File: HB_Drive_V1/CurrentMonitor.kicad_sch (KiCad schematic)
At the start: 0 parts

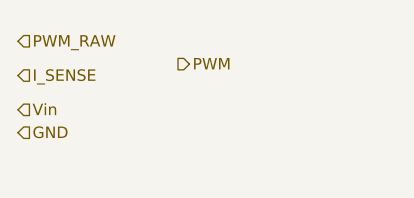
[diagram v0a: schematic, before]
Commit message: fixes git and adds a first revision of the Inner Current Regulator (NOT COMPLETE)
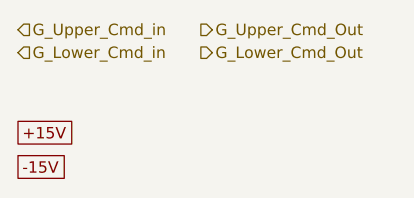
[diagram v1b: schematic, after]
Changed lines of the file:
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@@
 	(generator_version "10.0")
 	(paper "A4")
-	(hierarchical_label "GND"
+	(global_label "-15V"
+		(shape passive)
+		(at 88.9 87.63 0)
+		(fields_autoplaced yes)
+		(effects
+			(font
+				(size 1.27 1.27)
+			)
+			(justify left)
+		)
+		(property "Intersheetrefs" "${INTERSHEET_REFS}"
+			(at 95.8539 87.63 0)
+			(hide yes)
+			(show_name no)
+			(do_not_autoplace no)
+			(effects
+				(font
+					(size 1.27 1.27)
+				)
+				(justify left)
+			)
+		)
+	)
+	(global_label "+15V"
+		(shape passive)
+		(at 88.9 83.82 0)
+		(fields_autoplaced yes)
+		(effects
+			(font
+				(size 1.27 1.27)
+			)
+			(justify left)
+		)
+		(property "Intersheetrefs" "${INTERSHEET_REFS}"
+			(at 95.8539 83.82 0)
+			(hide yes)
+			(show_name no)
+			(do_not_autoplace no)
+			(effects
+				(font
+					(size 1.27 1.27)
+				)
+				(justify left)
+			)
+		)
+	)
+	(hierarchical_label "G_Lower_Cmd_in"
 		(shape input)
-		(at 88.9 83.82 0)
+		(at 88.9 74.93 0)
 		(effects
 			(font
@@
 		)
 	)
-	(hierarchical_label "I_SENSE"
-		(shape input)
-		(at 88.9 77.47 0)
+	(hierarchical_label "G_Lower_Cmd_Out"
+		(shape output)
+		(at 109.22 74.93 0)
 		(effects
 			(font
@@
 		)
 	)
-	(hierarchical_label "PWM_RAW"
+	(hierarchical_label "G_Upper_Cmd_in"
 		(shape input)
-		(at 88.9 73.66 0)
+		(at 88.9 72.39 0)
 		(effects
 			(font
@@
 		)
 	)
-	(hierarchical_label "Vin"
-		(shape input)
-		(at 88.9 81.28 0)
+	(hierarchical_label "G_Upper_Cmd_Out"
+		(shape output)
+		(at 109.22 72.39 0)
 		(effects
 			(font
-				(size 1.27 1.27)
-			)
-			(justify left)
-		)
-	)
-	(hierarchical_label "PWM"
-		(shape output)
-		(at 106.68 76.2 0)
-		(effects
-			(font

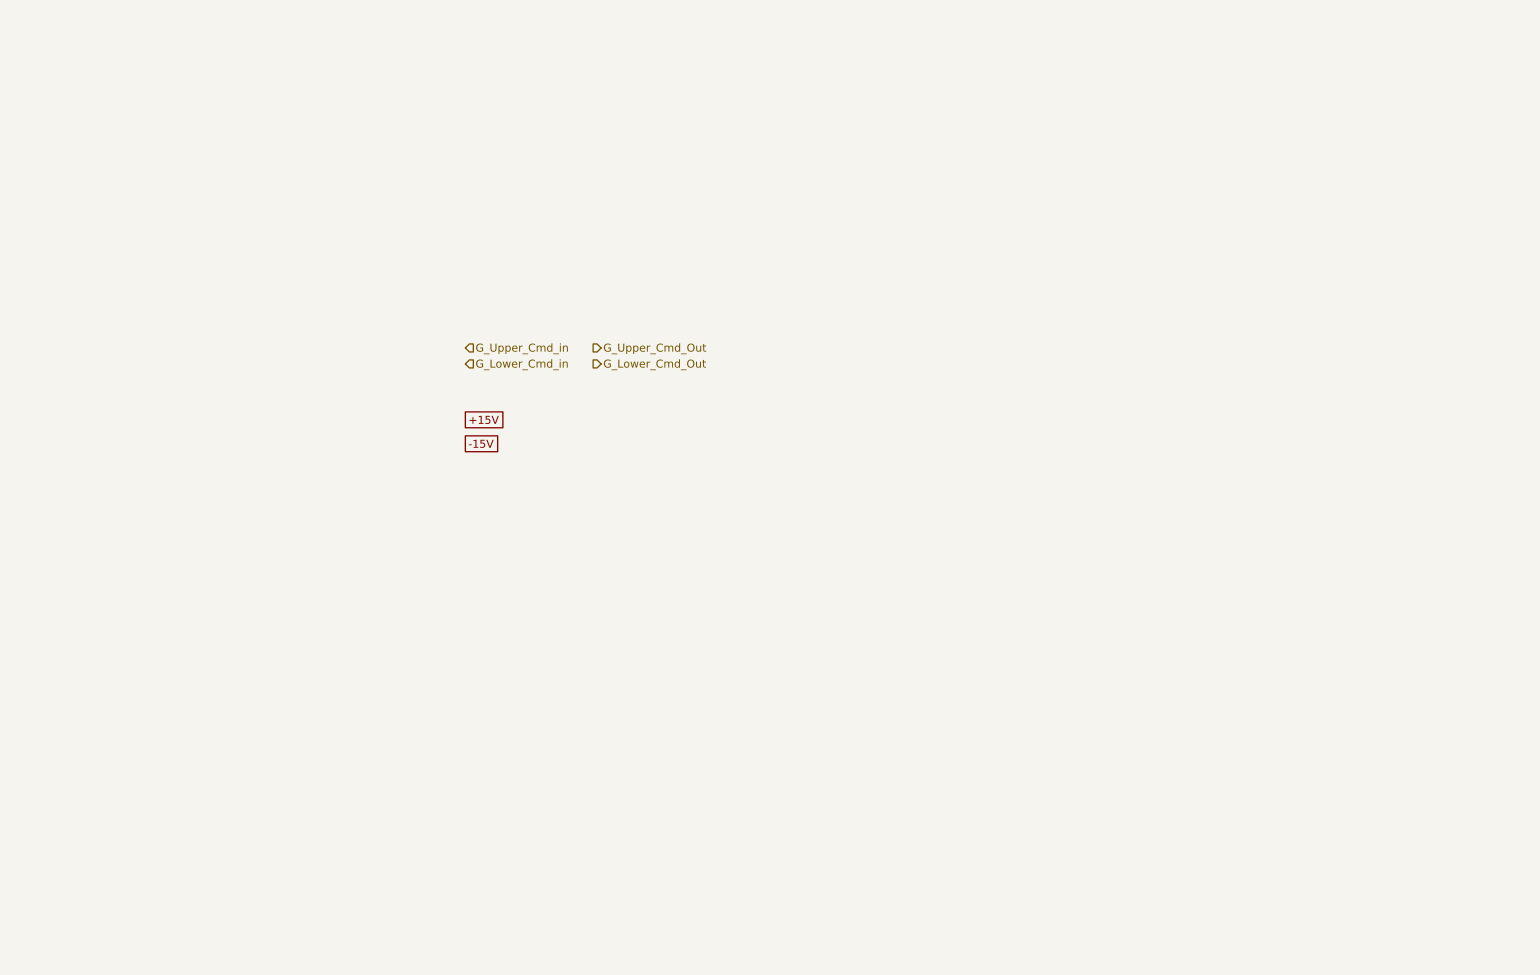
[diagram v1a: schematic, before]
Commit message: adds 10v reference and DC offsets / gain control to I_fdbk and V_fdbk
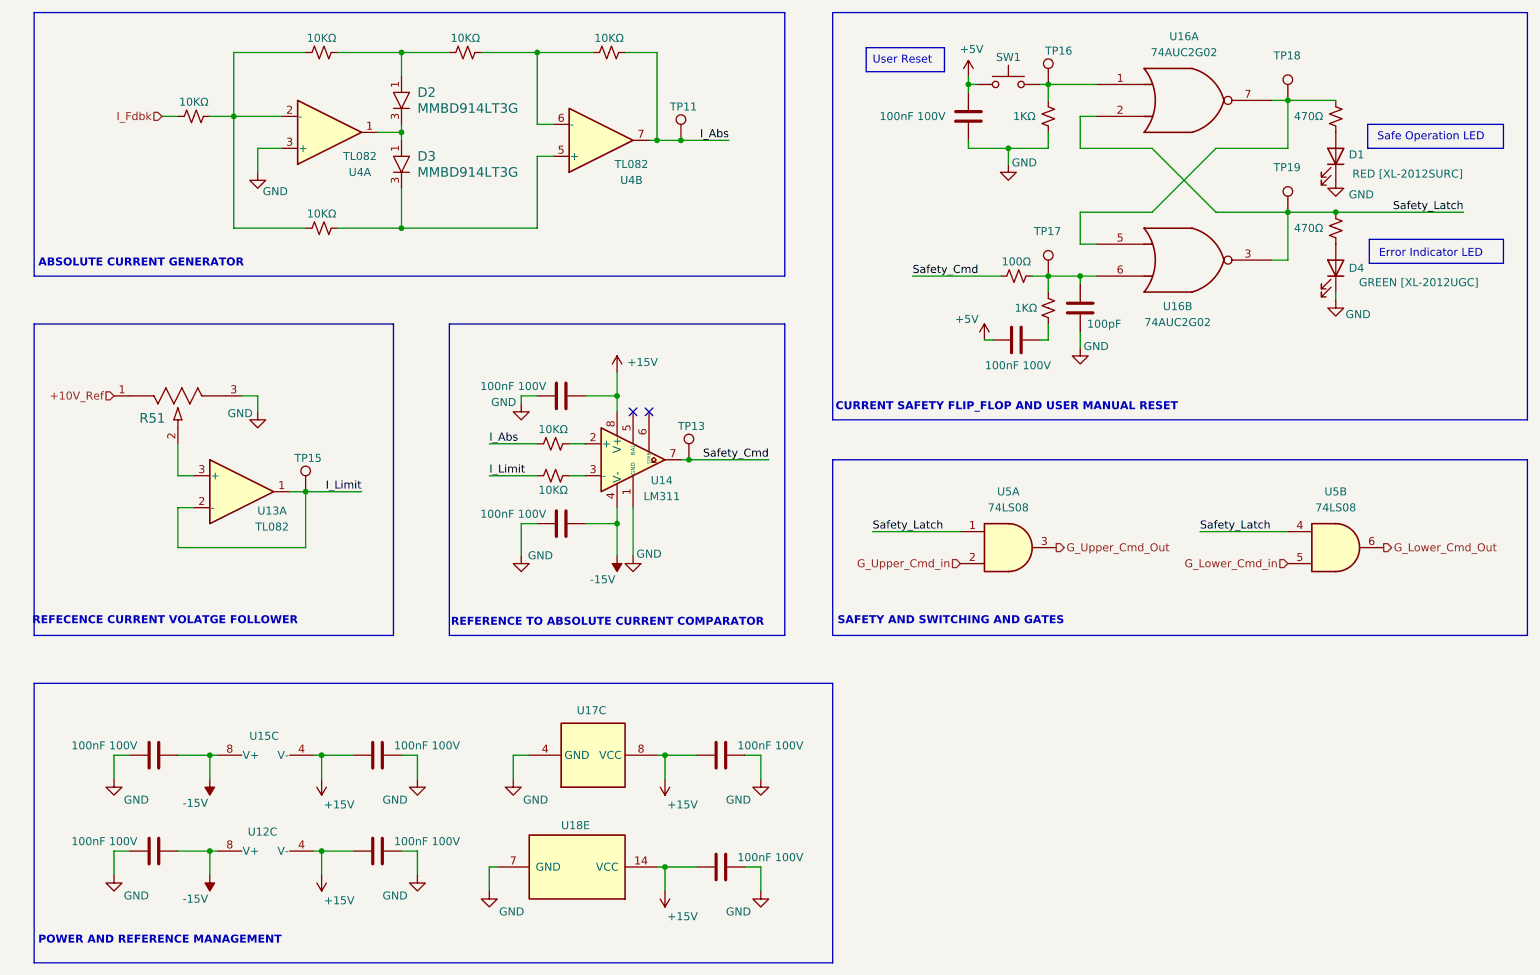
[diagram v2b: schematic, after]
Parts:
- added C25, C26, C28, C29, C30, C31, C34, C35, C36, C37: 100nF 100V, Capacitor_SMD:C_0603_1608Metric, symbol Device:C
- added C32: 100pF, Capacitor_SMD:C_0603_1608Metric, symbol Device:C
- added D1: RED [XL-2012SURC], LED_SMD:LED_0805_2012Metric_Pad1.15x1.40mm_HandSolder, symbol Device:LED
- added D2, D3: MMBD914LT3G, Package_TO_SOT_SMD:SOT-23-3, symbol MMBD914LT3G:MMBD914LT3G
- added D4: GREEN [XL-2012UGC], LED_SMD:LED_0805_2012Metric_Pad1.15x1.40mm_HandSolder, symbol Device:LED
- added R25, R26, R27, R47, R48, R60, R61: 10KΩ, Resistor_SMD:R_0603_1608Metric_Pad0.98x0.95mm_HandSolder, symbol Device:R_Small_US
- added R51: PV36W104C01B00, PV36W104C01B00:POT_PV36W_BRN, symbol PV36W104C01B00:PV36W104C01B00
- added R62, R64: 1KΩ, Resistor_SMD:R_0603_1608Metric_Pad0.98x0.95mm_HandSolder, symbol Device:R_Small_US
- added R63: 100Ω, Resistor_SMD:R_0603_1608Metric_Pad0.98x0.95mm_HandSolder, symbol Device:R_Small_US
- added R65, R66: 470Ω, Resistor_SMD:R_0603_1608Metric_Pad0.98x0.95mm_HandSolder, symbol Device:R_Small_US
- added SW1: SW_Push, symbol Switch:SW_Push
- added TP11, TP13, TP15, TP16, TP17, TP18, TP19: TestPoint, TestPoint:TestPoint_Loop_D2.60mm_Drill1.6mm_Beaded, symbol Connector:TestPoint
- added U12, U13, U15, U4: TL082, Package_SO:SOIC-8_5.3x5.3mm_P1.27mm, symbol Amplifier_Operational:TL082
- added U14: LM311, symbol Comparator:LM311
- added U16, U17: 74AUC2G02, symbol 74xGxx:74AUC2G02
- added U18, U5: 74LS08, symbol 74xx:74LS08
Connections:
- net +15V: now also C28.1, C34.2, C35.2, C36.2, C37.2, U12.4 (V-), U14.8 (V+), U15.4 (V-), U17.8 (VCC), U18.14 (VCC)
- net -15V: now also C25.1, C26.1, C29.1, U12.8 (V+), U14.4 (V-), U15.8 (V+)
- net G_Lower_Cmd_Out: now also U5.6
- net G_Lower_Cmd_in: now also U5.5
- net G_Upper_Cmd_Out: now also U5.3
- net G_Upper_Cmd_in: now also U5.2
- new net: C31.2, R64.1
- new net: C32.2, R63.2, R64.2, TP17.1, U16.6
- new net: D4.2 (A), R65.1
- new net: R25.2, R26.1, R27.1, U4.2 (-)
- new net: D3.3, R27.2, U4.5 (+)
- new net: D1.2 (A), R66.1
- new net: D2.1, R26.2, R47.1
- new net: R47.2, R48.1, U4.6 (-)
- new net: R66.2, TP18.1, U16.5, U16.7
- new net: D2.3, D3.1, U4.1
- new net: R51.2, U13.3 (+)
- new net: R60.2, U14.2 (+)
- new net: R62.2, SW1.2, TP16.1, U16.1
- new net: R61.1, U14.3 (-)
- new net +10V_Ref: R51.1
- new net +5V: C30.1, C31.1, SW1.1
- new net GND: C25.2, C26.2, C28.2, C29.2, C30.2, C32.1, C34.1, C35.1, C36.1, C37.1, D1.1 (K), D4.1 (K), R51.3, R62.1, U14.1 (GND), U17.4 (GND), U18.7 (GND), U4.3 (+)
- new net I_Abs: R48.2, R60.1, TP11.1, U4.7
- new net I_Fdbk: R25.1
- new net I_Limit: R61.2, TP15.1, U13.1, U13.2 (-)
- new net Safety_Cmd: R63.1, TP13.1, U14.7
- new net Safety_Latch: R65.2, TP19.1, U16.2, U16.3, U5.1, U5.4
- no-connect marks 0 -> 2
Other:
- note added: "ABSOLUTE CURRENT GENERATOR"
- note added: "CURRENT SAFETY FLIP_FLOP AND USER MANUAL RESET"
- note added: "Error Indicator LED"
- note added: "POWER AND REFERENCE MANAGEMENT"
- note added: "REFECENCE CURRENT VOLATGE FOLLOWER"
- note added: "REFERENCE TO ABSOLUTE CURRENT COMPARATOR"
- note added: "SAFETY AND SWITCHING AND GATES"
- note added: "Safe Operation LED"
- note added: "User Reset"
